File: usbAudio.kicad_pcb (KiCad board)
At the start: 2 copper layers, 45.2 x 15.6 mm, 35 parts, among them J1 USB_B_Micro, J2 54-00176, U1 PCM2906CDBR, U2 MAX9814, U3 TCR2EF36, Y1 12MHz

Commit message: Update design and readme
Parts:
- removed AMP: Jumper_NC_Small, Jumper:SolderJumper-2_P1.3mm_Bridged_RoundedPad1.0x1.5mm
- removed the C6 at (91.0, 78.3)
- removed D1: D_Schottky_Small, Diode_SMD:D_SOD-523
- removed GND, MIC: Jumper_NO_Small, Jumper:SolderJumper-2_P1.3mm_Open_RoundedPad1.0x1.5mm
- removed the R7 at (71.1, 80.3)
- removed the R8 at (71.1, 81.8)
- added C1: 0.1uF, Capacitor_SMD:C_0603_1608Metric_Pad1.08x0.95mm_HandSolder, F.Cu at (72.1, 75.9)
- added C13: 1uF, Capacitor_SMD:C_0603_1608Metric_Pad1.08x0.95mm_HandSolder, F.Cu at (73.0, 86.1)
- added C16: 1uF, Capacitor_SMD:C_0603_1608Metric_Pad1.08x0.95mm_HandSolder, F.Cu at (71.4, 86.1)
- added C17: 1uF, Capacitor_SMD:C_0603_1608Metric_Pad1.08x0.95mm_HandSolder, F.Cu at (69.8, 86.1)
- added J2: Conn_01x03, Package_TO_SOT_THT:TO-92Flat, F.Cu at (74.4, 74.1)
- added JP2: Jumper_NO_Small, Jumper:SolderJumper-2_P1.3mm_Open_RoundedPad1.0x1.5mm, F.Cu at (58.6, 76.7)
- added U4: MIC5365-3.3YD5, Package_TO_SOT_SMD:SOT-23-5, F.Cu at (70.4, 82.2)
- U3: footprint Package_TO_SOT_SMD:TSOT-23-5 -> Package_TO_SOT_SMD:SOT-23-5
- moved JP1 12.5 mm to (69.5, 74.6), turned to 180 degrees
- moved R1 11.4 mm to (68.3, 86.1), turned to -90 degrees
- moved R8 9.12 mm to (61.6, 77.1), turned to 0 degrees
- moved C3 7.89 mm to (74.0, 77.9), turned to 90 degrees
- moved C2 6.84 mm to (61.6, 73.9), turned to 180 degrees
- moved R7 6.84 mm to (61.6, 78.7)
- moved R6 3.92 mm to (91.1, 77.6)
- moved C8 3.82 mm to (70.3, 77.7), turned to -90 degrees
- moved C4 3.17 mm to (61.6, 75.4)
- moved C5 1.95 mm to (76.4, 77.9)
- moved J3 1.92 mm to (55.2, 83.0)
- moved U2 1.86 mm to (65.5, 74.9)
- moved C6 1.86 mm to (65.6, 77.5)
- moved C7 1.64 mm to (68.8, 77.7), turned to -90 degrees
- moved U3 1.24 mm to (74.8, 82.2)
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- renumbered C13 to C14, C14 to C15, C3 to C2, C8 to C3, C1 to C4, C2 to C6, C4 to C7, C7 to C8, J2 to J3, VCC to JP1, R3 to R4, R4 to R5, R5 to R6, R2 to R7, R6 to R8
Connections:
- net /MICIN renamed Net-(C2-Pad1)
- net SSPND* renamed /*SSPND
- C3 pad 1: VCCCI -> /VCCCI
- C8 pad 1: VCCCI -> /VCCCI
- J1 pad 10: GND -> (no net)
- J1 pad 11: GND -> (no net)
- J1 pad S_1: GND -> (no net)
- J1 pad S_2: GND -> (no net)
- J1 pad S_3: GND -> (no net)
- J1 pad S_4: GND -> (no net)
- JP1 pad 2: VCCCI -> /VCCCI
- R1 pad 1: Net-(R1-Pad1) -> /VBIAS
- R8 pad 1: Net-(R1-Pad1) -> Net-(JP2-Pad1)
- U1 pad 10: VCCCI -> /VCCCI
- U1 pad 12: Net-(JP1-Pad2) -> Net-(C1-Pad1)
- U1 pad 13: Net-(JP1-Pad2) -> /IN_R
- U2 pad 13: Net-(R1-Pad1) -> Net-(JP2-Pad1)
- U2 pad 5: VCCCI -> /VCCCI
- U3 pad 4: Net-(R7-Pad2) -> unconnected-(U3-Pad4)
- U3 pad 5: Net-(D1-Pad2) -> /VCCCI
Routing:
- net VCCCI: track 56.5 -> 0.00 mm, vias 2 -> 0
- net /VCCCI: track 0.00 -> 35.3 mm
- net Net-(C2-Pad1): track 20.6 -> 1.34 mm
- net /VBIAS: track 0.00 -> 18.5 mm
- net Net-(R1-Pad1): track 17.1 -> 0.00 mm
- net MIC+: track 14.0 -> 28.6 mm
- net Net-(JP1-Pad1): track 5.09 -> 18.3 mm, vias 0 -> 2
- net Net-(JP1-Pad2): track 12.6 -> 0.00 mm
- net Net-(C1-Pad1): track 0.00 -> 10.8 mm
- net Net-(R7-Pad1): track 11.9 -> 4.08 mm
- net Net-(JP2-Pad1): track 0.00 -> 6.41 mm
- net Net-(D1-Pad2): track 6.04 -> 0.00 mm
- net /IN_R: track 0.00 -> 4.05 mm
- net Net-(R7-Pad2): track 3.43 -> 0.00 mm
- net /*SSPND: track 42.0 -> 45.3 mm
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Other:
- board size 45.2 x 15.6 mm -> 42.6 x 14.9 mm
- board text added: "BIAS"
- board text added: "GAIN"

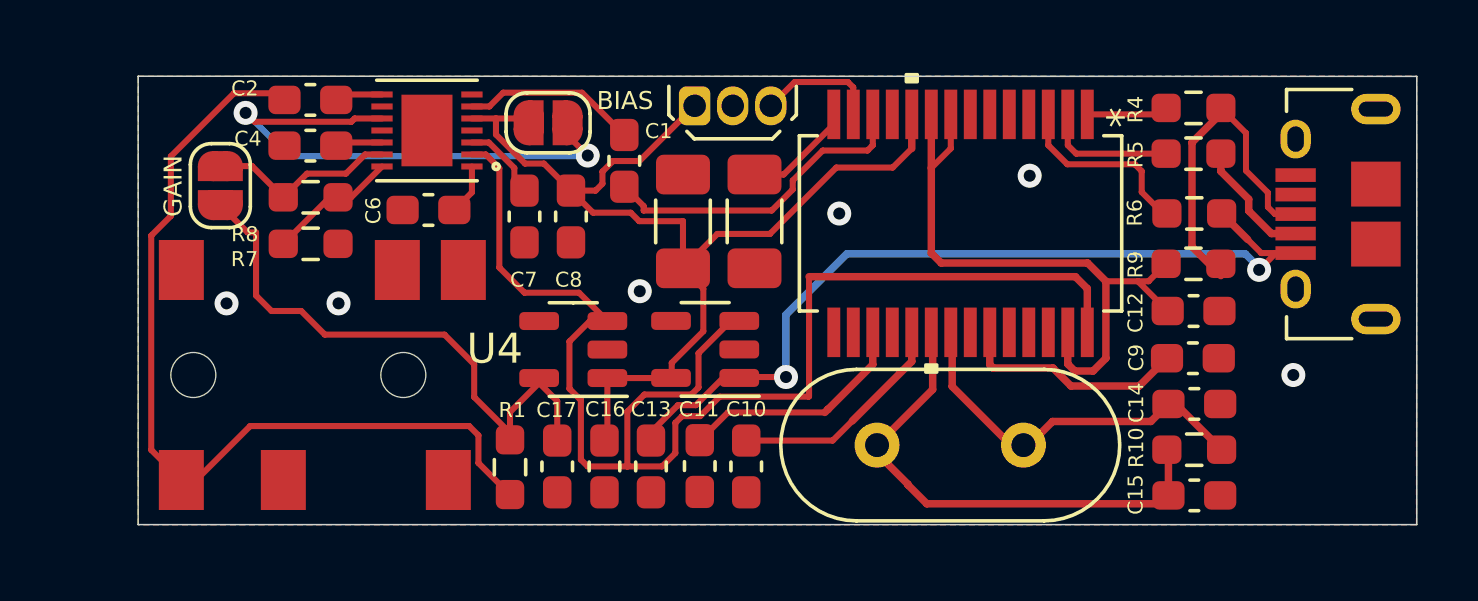
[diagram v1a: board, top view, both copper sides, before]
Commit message: Updates from reddit feedback https://www.reddit.com/r/PrintedCircuitBoard/comments/so21cn/project_review_usb_microphone_interface/
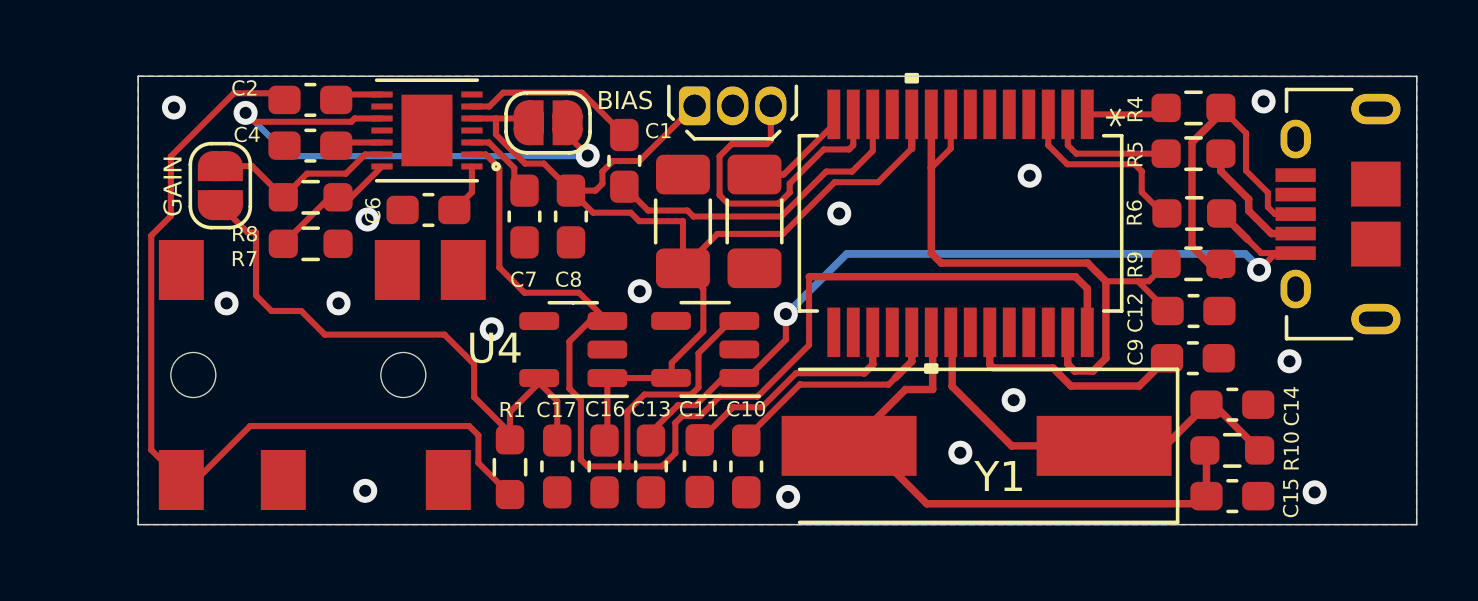
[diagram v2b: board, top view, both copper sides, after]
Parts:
- Y1: footprint Crystal:Crystal_HC49-U_Vertical -> Crystal:Crystal_SMD_HC49-SD
- moved Y1 1.56 mm to (83.8, 85.4)
- moved C14 1.27 mm to (92.4, 84.0)
- moved C15 1.27 mm to (92.4, 87.1)
- moved R10 1.27 mm to (92.4, 85.5)
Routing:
- net /IN_R: track 4.05 -> 11.0 mm
- net /XTO: track 16.8 -> 19.4 mm
- net /*SSPND: track 45.3 -> 44.3 mm
- net VBUS: track 27.2 -> 26.4 mm
- net GND: vias 6 -> 15

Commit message: Changes for JLC production. Add mounting hole.
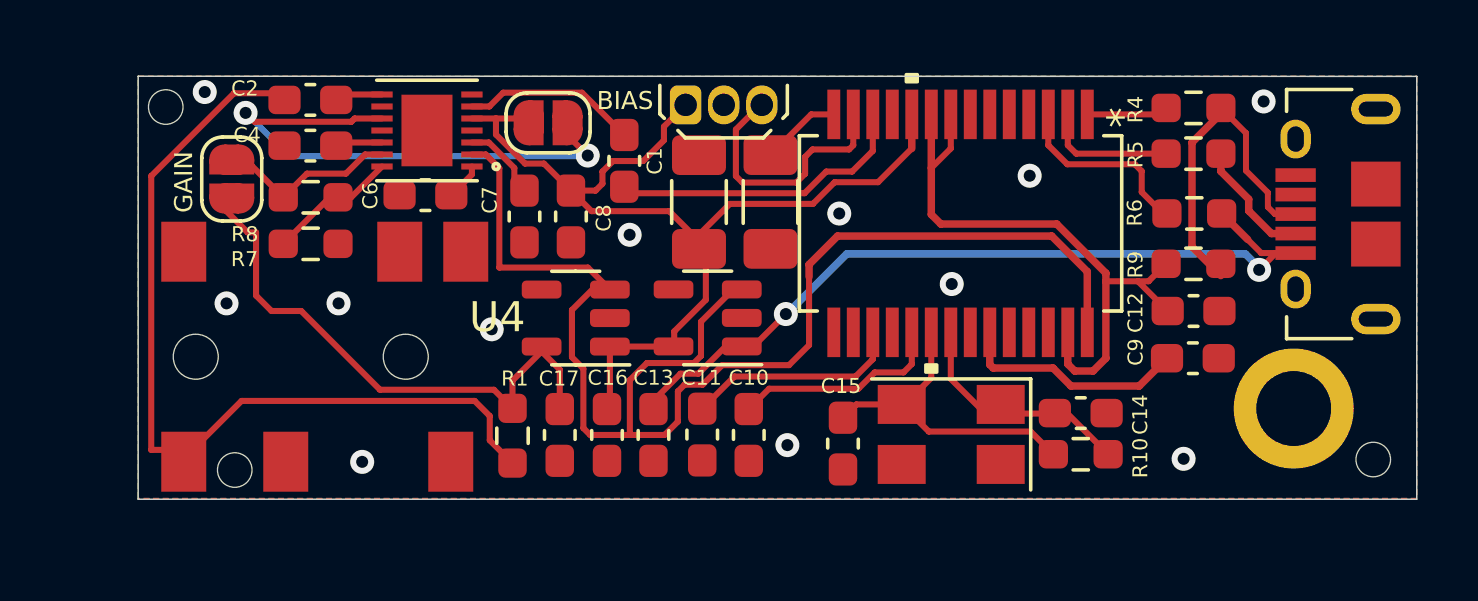
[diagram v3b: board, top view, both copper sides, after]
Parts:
- added ALIGN1: MountingHole_2.1mm, MountingHole:MountingHole_2.1mm, F.Cu at (97.0, 85.8)
- added ALIGN2: MountingHole_2.1mm, MountingHole:MountingHole_2.1mm, F.Cu at (59.1, 86.2)
- added REF**: MountingHole_2.1mm, MountingHole:MountingHole_2.1mm, F.Cu at (56.8, 74.1)
- added REF**: MountingHole_2.5mm_Pad, MountingHole:MountingHole_2.5mm_Pad, F.Cu at (94.4, 84.2)
- C14, C15: value 1uF -> 30pF
- U4: value MIC5365-3.3YD5 -> MIC5365-3.0YD5-TR
- Y1: footprint Crystal:Crystal_SMD_HC49-SD -> Crystal:Crystal_SMD_5032-4Pin_5.0x3.2mm
- moved C15 13.1 mm to (79.4, 85.3), turned to -90 degrees
- moved C14 5.06 mm to (87.3, 84.3)
- moved R10 5.05 mm to (87.3, 85.7)
- moved C13 1.05 mm to (73.1, 85.0)
- moved C16 1.05 mm to (71.5, 85.0)
- moved C17 1.05 mm to (69.9, 85.0)
- moved U3 1.05 mm to (74.9, 81.1)
- moved U4 1.05 mm to (70.5, 81.1)
- moved C11 1.05 mm to (74.7, 85.0)
- moved R1 1.05 mm to (68.4, 85.1)
- moved C10 1.05 mm to (76.2, 85.0)
- moved Y1 0.93 mm to (83.0, 85.0)
- moved C3 0.84 mm to (74.6, 77.3)
- moved C5 0.84 mm to (77.0, 77.3)
- moved J3 0.61 mm to (55.3, 82.4)
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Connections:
- net /VDDI renamed VDD
- C16 pad 1: /VCCCI -> VCC
- C3 pad 1: /VCCCI -> VCC
- C8 pad 1: /VCCCI -> VCC
- J2 pad 1: /VCCCI -> VCC
- JP1 pad 1: Net-(JP1-Pad1) -> VCC
- JP1 pad 2: /VCCCI -> Net-(JP1-Pad2)
- U1 pad 10: /VCCCI -> VCC
- U2 pad 10: Net-(JP1-Pad1) -> Net-(JP1-Pad2)
- U2 pad 5: /VCCCI -> VCC
- U3 pad 5: /VCCCI -> VCC
- U4 pad 1: /VCCCI -> VCC
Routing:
- net /VCCCI: track 35.3 -> 0.00 mm
- net VCC: track 0.00 -> 32.6 mm
- net Net-(JP1-Pad2): track 0.00 -> 17.9 mm, vias 0 -> 2
- net Net-(JP1-Pad1): track 17.9 -> 0.00 mm, vias 2 -> 0
- net /XTO: track 19.4 -> 11.3 mm
- net /XTI: track 12.0 -> 7.44 mm
- net /IN_R: track 11.0 -> 8.59 mm
- net Net-(C10-Pad2): track 8.54 -> 7.11 mm
- net VBUS: track 26.4 -> 25.3 mm
- net Net-(C1-Pad1): track 10.8 -> 9.87 mm
- net /VBIAS: track 18.5 -> 17.7 mm
- net Net-(C5-Pad1): track 3.33 -> 2.67 mm
- net Net-(C11-Pad2): track 7.87 -> 7.27 mm
- net VDD: track 21.7 -> 21.1 mm
- net GND: vias 15 -> 12
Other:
- board size 42.6 x 14.9 mm -> 42.6 x 14.1 mm

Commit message: Fix crystal pin mappings (1 and 3 instead of 1 and 2)
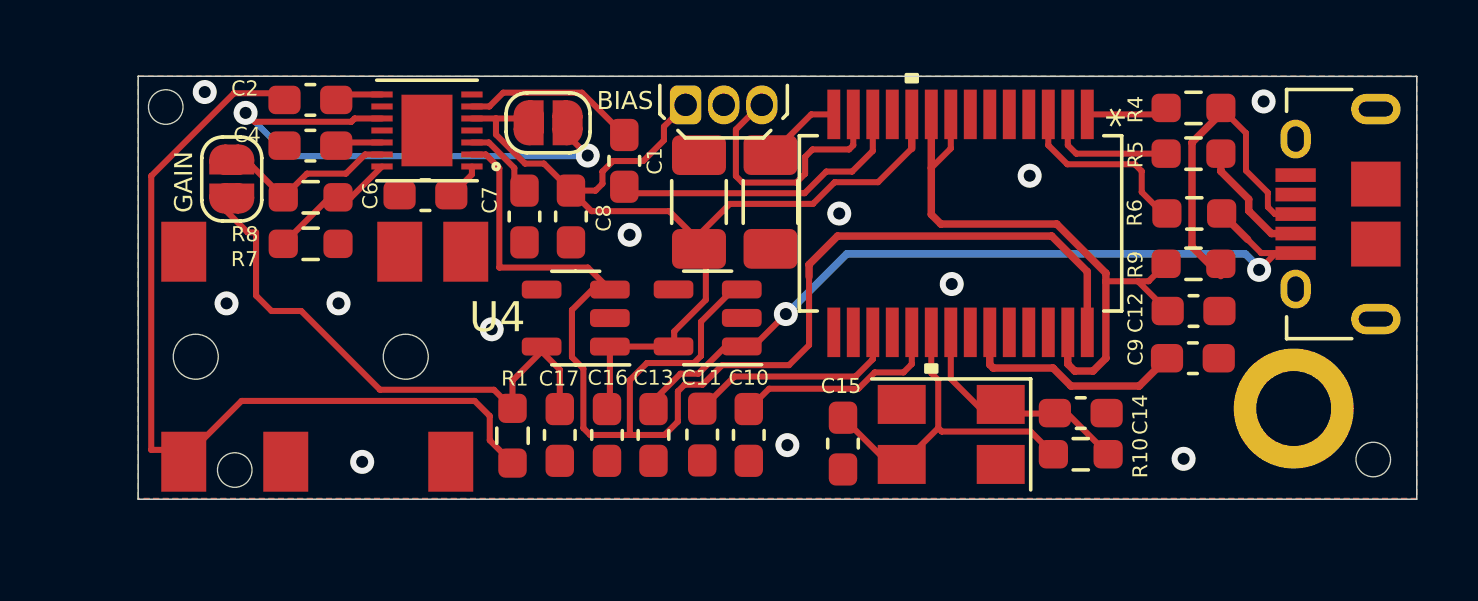
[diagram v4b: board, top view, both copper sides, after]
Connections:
- Y1 pad 2: /XTO -> (no net)
- Y1 pad 3: (no net) -> /XTO
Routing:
- net /XTO: track 11.3 -> 11.8 mm
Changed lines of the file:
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@@
     (property "Sheetfile" "usbAudio.kicad_sch")
     (property "Sheetname" "")
-    (attr through_hole exclude_from_pos_files exclude_from_bom)
+    (attr through_hole exclude_from_pos_files)
     (fp_text reference "U1" (at 0 0 90) (layer "F.SilkS") hide
       (effects (font (size 1 1) (thickness 0.15)))
@@
     (pad "1" smd rect (at -1.65 1 180) (size 1.6 1.3) (layers "F.Cu" "F.Paste" "F.Mask")
       (net 11 "/XTI") (pinfunction "1") (pintype "passive"))
-    (pad "2" smd rect (at 1.65 1 180) (size 1.6 1.3) (layers "F.Cu" "F.Paste" "F.Mask")
-      (net 12 "/XTO") (pinfunction "2") (pintype "passive"))
-    (pad "3" smd rect (at 1.65 -1 180) (size 1.6 1.3) (layers "F.Cu" "F.Paste" "F.Mask"))
+    (pad "2" smd rect (at 1.65 1 180) (size 1.6 1.3) (layers "F.Cu" "F.Paste" "F.Mask"))
+    (pad "3" smd rect (at 1.65 -1 180) (size 1.6 1.3) (layers "F.Cu" "F.Paste" "F.Mask")
+      (net 12 "/XTO") (pinfunction "3") (pintype "passive"))
     (pad "4" smd rect (at -1.65 -1 180) (size 1.6 1.3) (layers "F.Cu" "F.Paste" "F.Mask"))
     (model "${KICAD6_3DMODEL_DIR}/Crystal.3dshapes/Crystal_SMD_5032-4Pin_5.0x3.2mm.wrl"
@@
     (property "Sheetfile" "usbAudio.kicad_sch")
     (property "Sheetname" "")
-    (attr through_hole exclude_from_pos_files exclude_from_bom)
+    (attr through_hole exclude_from_pos_files)
     (fp_text reference "U2" (at 0.05 -0.05 180) (layer "F.SilkS") hide
       (effects (font (size 1 1) (thickness 0.15)))
@@
     (property "Sheetfile" "usbAudio.kicad_sch")
     (property "Sheetname" "")
-    (attr smd exclude_from_pos_files exclude_from_bom)
+    (attr smd exclude_from_pos_files)
     (fp_text reference "J3" (at 0.1 6.6 unlocked) (layer "F.SilkS") hide
       (effects (font (size 1 1) (thickness 0.15)))
@@
     (property "Sheetfile" "usbAudio.kicad_sch")
     (property "Sheetname" "")
-    (attr exclude_from_pos_files exclude_from_bom)
+    (attr exclude_from_pos_files)
     (fp_text reference "JP1" (at -2 0 90) (layer "F.SilkS") hide
       (effects (font (size 0.5 0.5) (thickness 0.125)))
@@
     (property "Sheetfile" "usbAudio.kicad_sch")
     (property "Sheetname" "")
-    (attr through_hole exclude_from_pos_files exclude_from_bom)
+    (attr through_hole exclude_from_pos_files)
     (fp_text reference "J2" (at 1.27 -1.45) (layer "F.SilkS") hide
       (effects (font (size 1 1) (thickness 0.15)))
@@
     (property "Sheetfile" "usbAudio.kicad_sch")
     (property "Sheetname" "")
-    (attr exclude_from_pos_files exclude_from_bom)
+    (attr exclude_from_pos_files)
     (fp_text reference "JP2" (at 0 -1.8 90) (layer "F.SilkS") hide
       (effects (font (size 1 1) (thickness 0.15)))
@@
     (property "Sheetfile" "usbAudio.kicad_sch")
     (property "Sheetname" "")
-    (attr smd exclude_from_pos_files exclude_from_bom)
+    (attr smd exclude_from_pos_files)
     (fp_text reference "U3" (at 0 -2.4) (layer "F.SilkS") hide
       (effects (font (size 1 1) (thickness 0.15)))
@@
     (property "Sheetfile" "usbAudio.kicad_sch")
     (property "Sheetname" "")
-    (attr smd exclude_from_pos_files exclude_from_bom)
+    (attr smd exclude_from_pos_files)
     (fp_text reference "U4" (at 2.6162 0.0254) (layer "F.SilkS")
       (effects (font (size 1 1) (thickness 0.15)))
@@
   (segment (start 82.968 83.1628) (end 84.2762 84.471) (width 0.2032) (layer "F.Cu") (net 11))
   (segment (start 86.8407 84.3026) (end 88.2123 85.6742) (width 0.2032) (layer "F.Cu") (net 11))
-  (segment (start 79.375 84.4561) (end 79.8173 84.0138) (width 0.2032) (layer "F.Cu") (net 12))
-  (segment (start 81.3318 84.0138) (end 82.235311 84.917311) (width 0.2032) (layer "F.Cu") (net 12))
-  (segment (start 82.318002 83.129198) (end 80.9762 84.471) (width 0.2032) (layer "F.Cu") (net 12))
-  (segment (start 79.8173 84.0138) (end 81.3318 84.0138) (width 0.2032) (layer "F.Cu") (net 12))
-  (segment (start 82.318002 81.6102) (end 82.318002 83.129198) (width 0.2032) (layer "F.Cu") (net 12))
   (segment (start 85.630411 84.917311) (end 86.3873 85.6742) (width 0.2032) (layer "F.Cu") (net 12))
-  (segment (start 82.235311 84.917311) (end 85.630411 84.917311) (width 0.2032) (layer "F.Cu") (net 12))
+  (segment (start 82.55 84.8) (end 81.3362 86.0138) (width 0.2032) (layer "F.Cu") (net 12))
+  (segment (start 80.9327 86.0138) (end 79.375 84.4561) (width 0.2032) (layer "F.Cu") (net 12))
+  (segment (start 82.667311 84.917311) (end 85.630411 84.917311) (width 0.2032) (layer "F.Cu") (net 12))
+  (segment (start 82.318002 82.968002) (end 82.55 83.2) (width 0.2032) (layer "F.Cu") (net 12))
+  (segment (start 82.55 83.2) (end 82.55 84.8) (width 0.2032) (layer "F.Cu") (net 12))
+  (segment (start 82.55 84.8) (end 82.667311 84.917311) (width 0.2032) (layer "F.Cu") (net 12))
+  (segment (start 81.3362 86.0138) (end 81.3318 86.0138) (width 0.2032) (layer "F.Cu") (net 12))
+  (segment (start 81.3318 86.0138) (end 80.9327 86.0138) (width 0.2032) (layer "F.Cu") (net 12))
+  (segment (start 82.318002 81.6102) (end 82.318002 82.968002) (width 0.2032) (layer "F.Cu") (net 12))
   (segment (start 62.588101 75.281999) (end 64.0086 75.281999) (width 0.2032) (layer "F.Cu") (net 13))
   (segment (start 89.9298 74.3458) (end 87.518001 74.3458) (width 0.2032) (layer "F.Cu") (net 14))
